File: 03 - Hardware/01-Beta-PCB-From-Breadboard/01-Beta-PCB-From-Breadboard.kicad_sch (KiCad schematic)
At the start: 20 parts, among them J0 Screw_Terminal_01x02, J1 Conn_01x03_Male, J10 Screw_Terminal_01x03, J2 Conn_01x03_Male, J3 Conn_01x03_Male, J4 Conn_01x03_Male, J5 4P4C, J6 Conn_01x02_Male, J7 Conn_01x03_Male, J8 4P4C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

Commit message: Initialisation of the thesis
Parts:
- removed SW?: (no value), symbol Switch:SW_Reed_Opener
- added BT?: Battery, symbol Device:Battery
- added C?: 22uF, symbol Device:C_Polarized_Small
- added C?: 220n, symbol Device:C
- added R?: 10k, symbol Device:R
- added SC?: Solar_Cells, symbol Device:Solar_Cells
- added SW? (x2): Internal reed switch, symbol Switch:SW_Reed
- added U?: Wind vane RJ11, symbol RJ11-Connectors:RJ11-6P6C
- added U?: Anemometer, symbol RJ11-Connectors:RJ11-6P6C
- added U?: AMS1117-3.3, Package_TO_SOT_SMD:SOT-223-3_TabPin2, symbol Regulator_Linear:AMS1117-3.3
- added U?: BME280, BME280_Module:BME280_SPI, symbol BME280_Module:BME280_SPI
- added U?: STM32F103C8T6_BluePill, STM32-BluePill:YAAJ_BluePill_1, symbol STM32_BluePill:YAAJ_BluePill
- added U?: Anemometer, symbol Rotate_45:Anemometer
- R?: value (none) -> R
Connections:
- net +3V3: now also R?.1, U?.1 (VCC), U?.5 (CSB), U?.6 (SDO)
- net Anemometer: now also U?.28 (PA3)
- net DS18B20: now also U?.11 (PB3)
- net GND: now also C?.2, C?.2, SC?.2 (-), SW?.2, SW?.2, U?.1 (GND), U?.19 (GND), U?.2 (GND), U?.39 (GND), U?.40 (GND)
- net LoRa_Reset: now also U?.5 (PA8)
- net RTC_Alarm: now also U?.10 (PA15)
- net Rain Gauge: now also U?.26 (PA1)
- net SCL: now also U?.14 (PB6)
- net SDA: now also U?.15 (PB7)
- net UART_RX: now also U?.7 (PA10)
- net UART_TX: now also U?.6 (PA9)
- net Wind_Vane: now also U?.34 (PB1)
- net at R?.2: now also SW?.1
- new net: U?., U?.2
- new net: U?.3, U?.3
- new net: U?.4, U?.4
- new net: U?., U?.5
- new net: C?.1, R?.2, SW?.1
- new net +24V: U?.3 (VI)
- new net +3.3V: C?.1, U?.2 (VO), U?.20 (3V3), U?.38 (3V3)
- new net I2C SCL: U?.4 (SCK)
- new net I2C SDA: U?.3 (SDI)
- new net LoRa_Interrupt: U?.8 (PA11)
- new net SPI_MISO: U?.3 (PB14)
- new net SPI_MOSI: U?.4 (PB15)
- new net SPI_NSS: U?.1 (PB12)
- new net SPI_SCLK: U?.2 (PB13)
- no-connect marks 19 -> 45
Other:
- note added: "Battery managing circuit (4)"
- note added: "Comparator circuit (5)"
- note added: "Main supply"
- note added: "Main system"
- note added: "Microcontroller input"
- note added: "Power source switching circuit (7)"
- note added: "Reference voltage generator (6)"
- note added: "Reversed current blockage (3)"
- note added: "Reversed current blockage (8)"
- note added: "Switching circuit for battery charging unit (1)"
- note added: "Voltage converter circuit (2)"
- note added: "Voltage regulators"

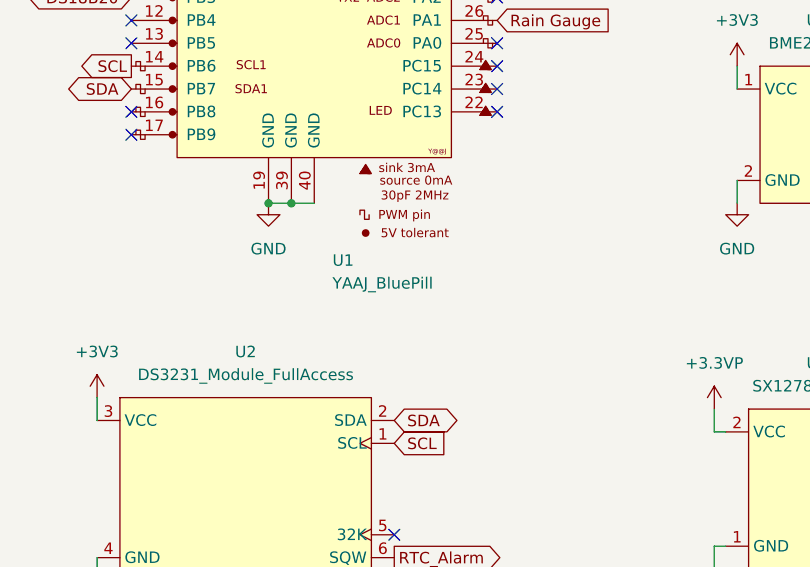
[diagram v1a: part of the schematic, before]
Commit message: New software version + new data
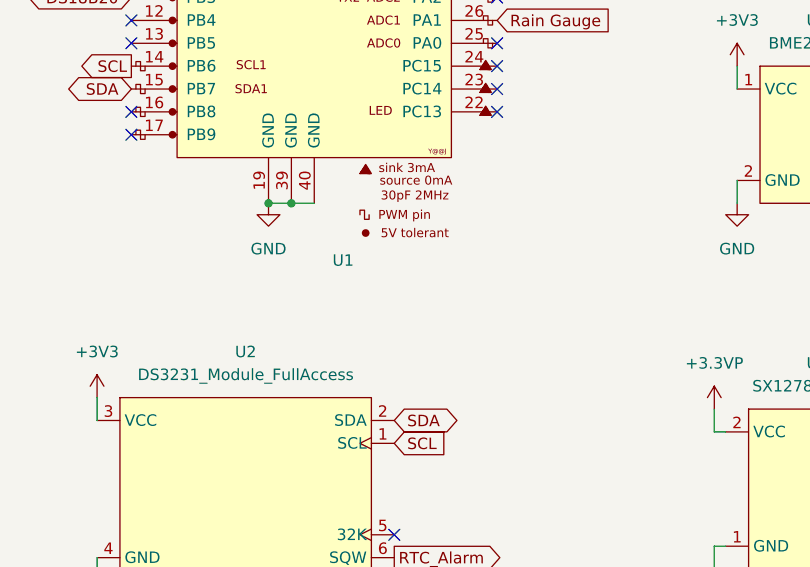
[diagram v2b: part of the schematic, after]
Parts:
- U1: value YAAJ_BluePill -> (none); footprint STM32-BluePill:YAAJ_BluePill_1 -> (none)
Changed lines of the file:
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@@
       (effects (font (size 1.27 1.27)) (justify left))
     )
-    (property "Value" "YAAJ_BluePill" (id 1) (at 60.4394 88.9 0)
+    (property "Value" "" (id 1) (at 60.4394 88.9 0)
       (effects (font (size 1.27 1.27)) (justify left))
     )
-    (property "Footprint" "STM32-BluePill:YAAJ_BluePill_1" (id 2) (at 56.515 27.94 90)
+    (property "Footprint" "" (id 2) (at 56.515 27.94 90)
       (effects (font (size 1.27 1.27)) hide)
     )

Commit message: 4
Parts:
- added C? (x3): (no value), symbol Device:C_Polarized
- added I? (x2): (no value), symbol pspice:ISOURCE
- added R? (x5): (no value), symbol Device:R
- added SW? (x2): SW, symbol Switch:SW_SPST
- added SW?: (no value), symbol Switch:SW_SPST
- U1: value (none) -> YAAJ_BluePill; footprint (none) -> STM32-BluePill:YAAJ_BluePill_1
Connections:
- net +3V3: now also R?.1
- net GND: now also C?.2, C?.2, C?.2, I?.2 (E2), I?.2 (E2), R?.2, R?.2, R?.2, R?.2
- new net: I?.1 (E1), R?.1, SW?.1 (A)
- new net: C?.1, SW?.2 (B) (x3)
- new net: I?.1 (E1), R?.1, R?.1, SW?.1 (A)
- new net: R?.1, R?.2, SW?.1 (A)
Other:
- note added: "V_{divider}"
